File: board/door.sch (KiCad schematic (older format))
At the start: 16 parts

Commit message: Finish first draft of schematic
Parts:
- removed C? (x2): C, symbol C
- removed D?: D_Photo, symbol D_Photo
- added C100u1, C? (x2): C, symbol C
- added D1: LED, symbol LED
- added J1: Conn_01x06, symbol Conn_01x06
- added R1: 10, symbol R
- added R2, R3, R5: R, symbol R
- added R4: R_PHOTO, symbol R_PHOTO
- added RV1: POT, symbol POT
- added U2: BA6287F-E2, symbol BA6287F-E2
- gave numbers to parts that had none: 13
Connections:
- net labels added: +5V, BOTTOM, FORWARD, GND, LED, LIGHT_SENS, MINUS, MISO, MODE, MOSI, OK, PLUS, REVERSE, SCK, TOP, XTAL1, XTAL2, ~RESET
- wire segments 0 -> 92
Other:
- note added: "32.786 kHz Crystal"
- note added: "4-Button Panel"
- note added: "General LED"
- note added: "ISP"
- note added: "LCD"
- note added: "Light Sensor"
- note added: "Magnetic Switches"
- note added: "Motor driver and DC Motor"
- note added: "Power Supply"
- moved on the sheet: BT1, C1, M1, SW_BOTTOM1, SW_MINUS1, SW_MODE1, SW_OK1, SW_PLUS1, SW_TOP1, U1, U3, U4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

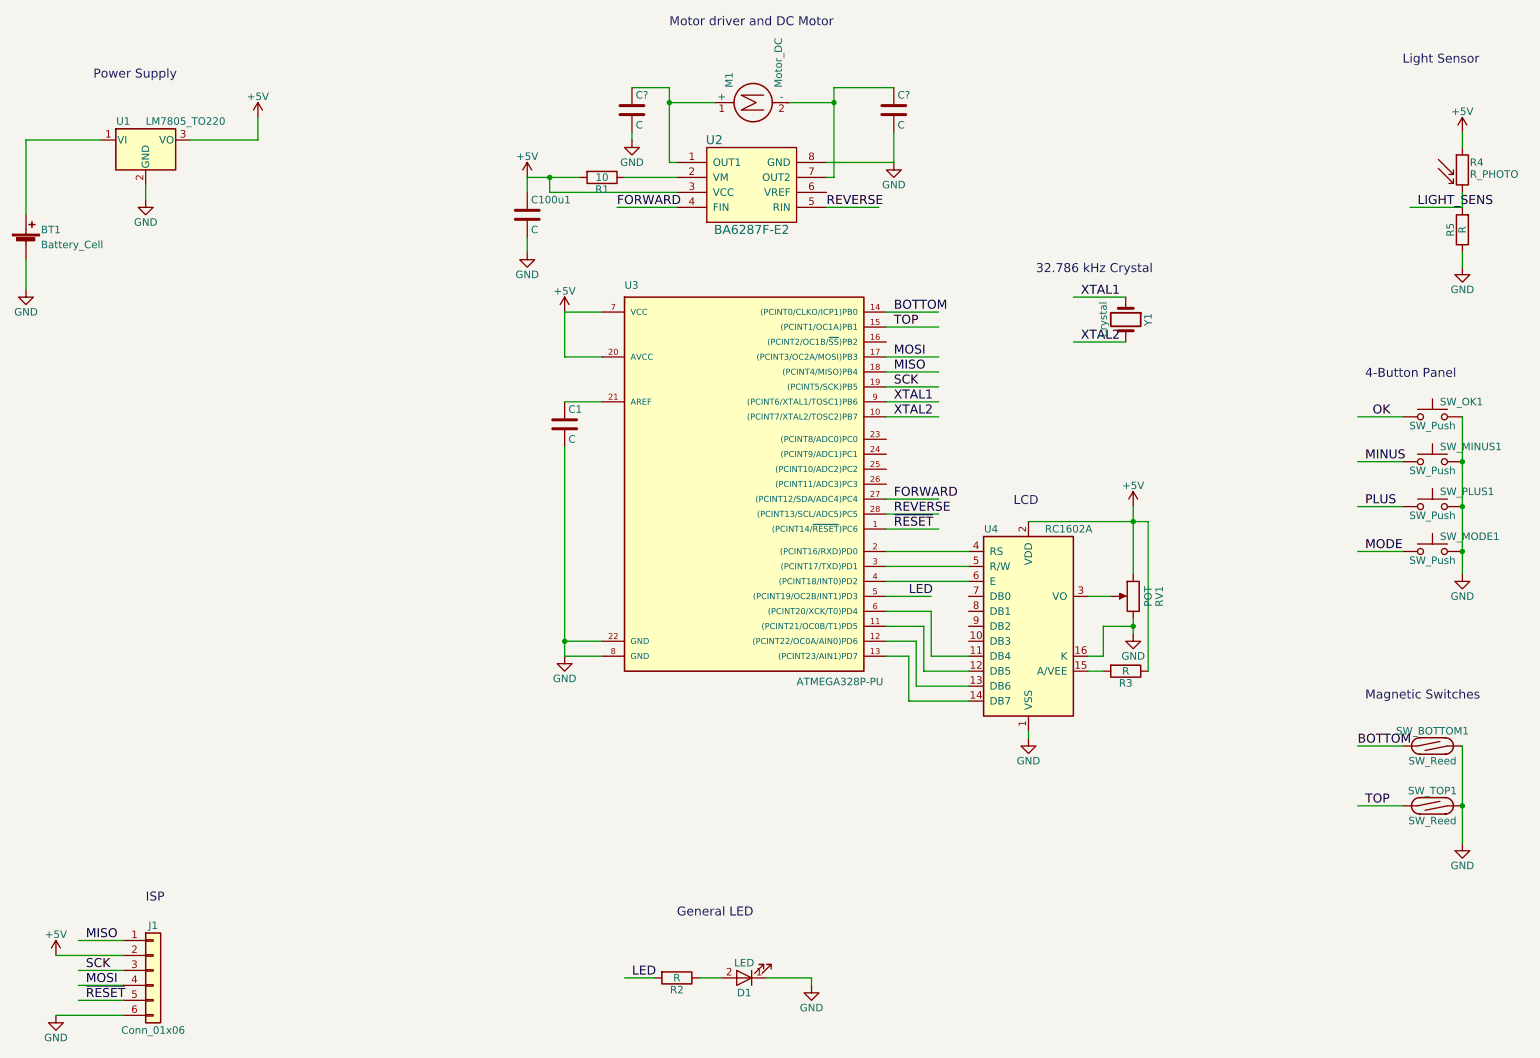
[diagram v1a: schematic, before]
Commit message: add schematic (missing)
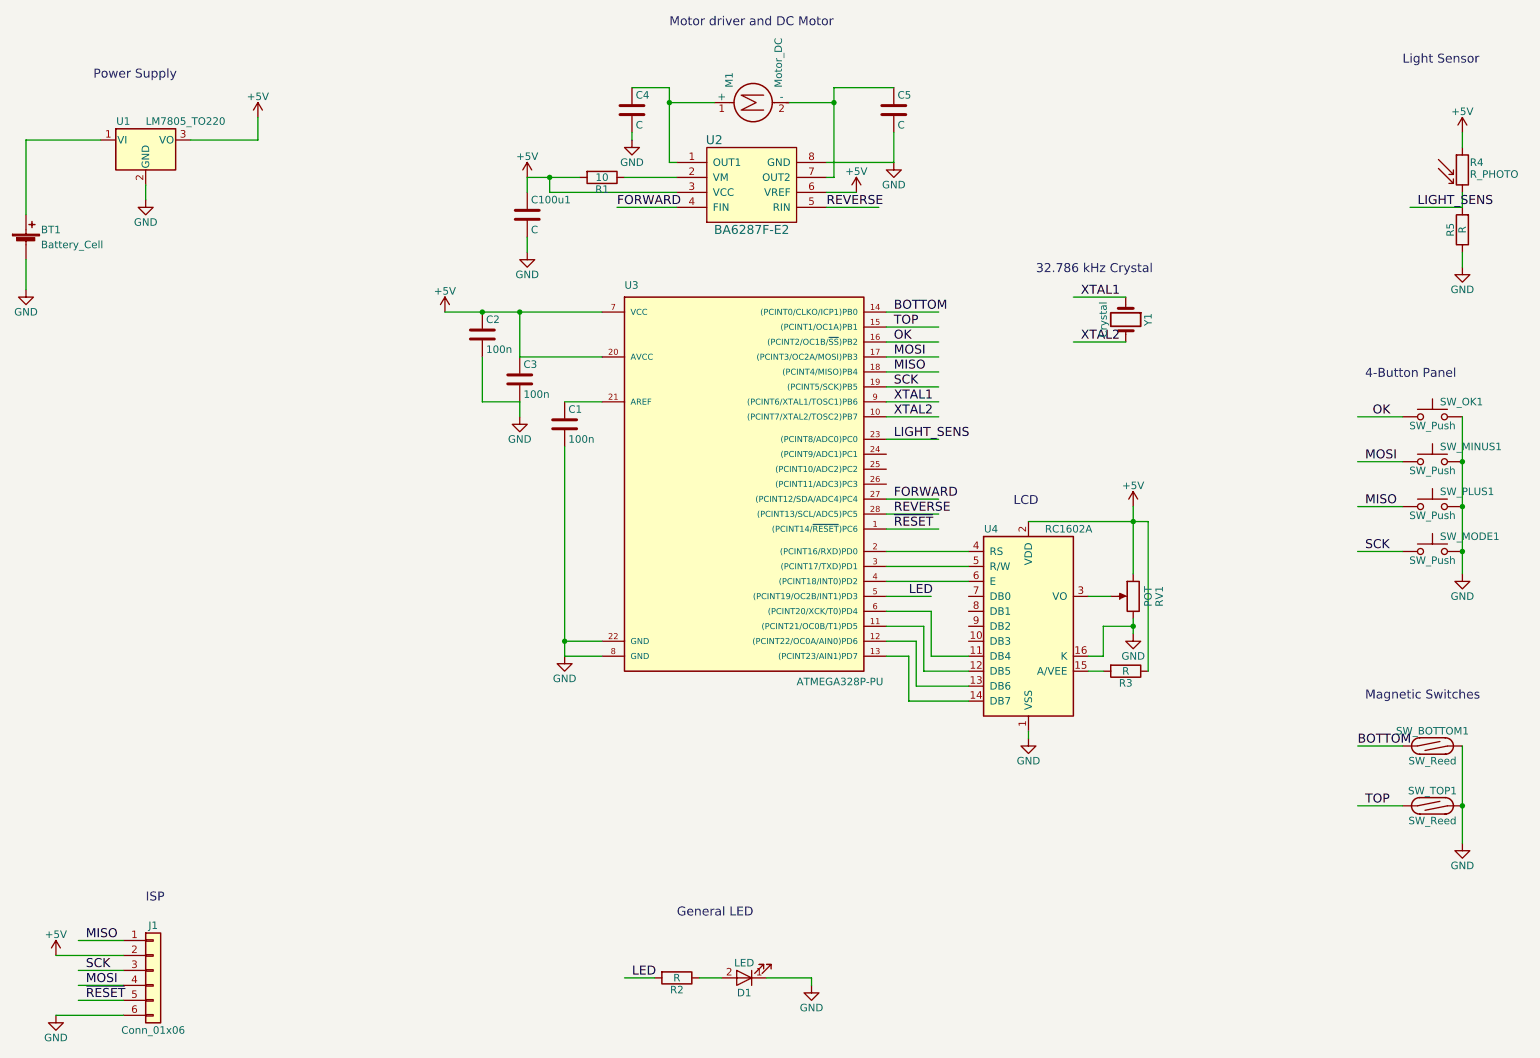
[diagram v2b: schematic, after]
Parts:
- added C2, C3: 100n, symbol C
- C1: value C -> 100n
- gave numbers to parts that had none: 2
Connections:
- net labels removed: MINUS, MODE, PLUS
- wire segments 92 -> 98
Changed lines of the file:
@@
 P 4500 3250
 F 0 "C1" H 4525 3350 50  0000 L CNN
-F 1 "C" H 4525 3150 50  0000 L CNN
+F 1 "100n" H 4525 3150 50  0000 L CNN
 F 2 "" H 4538 3100 50  0001 C CNN
 F 3 "" H 4500 3250 50  0001 C CNN
@@
 Wire Wire Line
 	6650 4300 7200 4300
-Wire Wire Line
-	8150 4400 8000 4400
 $Comp
 L GND #PWR03
@@
 	8300 4550 8300 4650
 Wire Wire Line
-	8100 4900 8000 4900
-Wire Wire Line
 	8000 4800 8100 4800
 Wire Wire Line
@@
 Wire Wire Line
 	4900 6950 5100 6950
-Wire Wire Line
-	7600 5300 7600 5350
 Text Label 4950 6950 0    60   ~ 0
 LED
-Wire Wire Line
-	900  1850 900  1350
-Wire Wire Line
-	900  1350 1400 1350
 $Comp
 L GND #PWR07
@@
 L +5V #PWR010
 U 1 1 5B279F52
-P 4500 2500
-F 0 "#PWR010" H 4500 2350 50  0001 C CNN
-F 1 "+5V" H 4500 2640 50  0000 C CNN
-F 2 "" H 4500 2500 50  0001 C CNN
-F 3 "" H 4500 2500 50  0001 C CNN
-	1    4500 2500
-	1    0    0    -1
-$EndComp
-Wire Wire Line
-	4750 2500 4500 2500
-Wire Wire Line
-	4750 2800 4500 2800
-Wire Wire Line
-	4500 2800 4500 2500
+P 3700 2500
+F 0 "#PWR010" H 3700 2350 50  0001 C CNN
+F 1 "+5V" H 3700 2640 50  0000 C CNN
+F 2 "" H 3700 2500 50  0001 C CNN
+F 3 "" H 3700 2500 50  0001 C CNN
+	1    3700 2500
+	1    0    0    -1
+$EndComp
+Wire Wire Line
+	4200 2800 4750 2800
 Wire Wire Line
 	6250 1500 6700 1500
@@
 OK
 Text Label 9850 3500 0    60   ~ 0
-MINUS
+MOSI
 Text Label 9850 3800 0    60   ~ 0
-PLUS
+MISO
 Text Label 9850 4100 0    60   ~ 0
-MODE
+SCK
 Wire Wire Line
 	1550 6700 1250 6700
@@
 	0    1    1    0
 $EndComp
-Wire Wire Line
-	4900 1600 5250 1600
 Wire Wire Line
 	4250 1600 4600 1600
@@
 Magnetic Switches
 $Comp
-L C C?
+L C C4
 U 1 1 5B28EE99
 P 4950 1150
-F 0 "C?" H 4975 1250 50  0000 L CNN
+F 0 "C4" H 4975 1250 50  0000 L CNN
 F 1 "C" H 4975 1050 50  0000 L CNN
 F 2 "" H 4988 1000 50  0001 C CNN
@@
 $EndComp
 $Comp
-L C C?
+L C C5
 U 1 1 5B28EF76
 P 6700 1150
-F 0 "C?" H 6725 1250 50  0000 L CNN
+F 0 "C5" H 6725 1250 50  0000 L CNN
 F 1 "C" H 6725 1050 50  0000 L CNN
 F 2 "" H 6738 1000 50  0001 C CNN
@@
 $EndComp
 $Comp
-L GND #PWR?
+L GND #PWR018
 U 1 1 5B28F12C
 P 4950 1350
-F 0 "#PWR?" H 4950 1100 50  0001 C CNN
+F 0 "#PWR018" H 4950 1100 50  0001 C CNN
 F 1 "GND" H 4950 1200 50  0000 C CNN
 F 2 "" H 4950 1350 50  0001 C CNN
@@
 $EndComp
 Wire Wire Line
-	4950 1300 4950 1350
-Wire Wire Line
 	4950 1000 5200 1000
 Connection ~ 5200 1100
@@
 	4500 3100 4750 3100
 $Comp
-L GND #PWR?
+L GND #PWR019
 U 1 1 5B28F5CD
 P 4500 4800
-F 0 "#PWR?" H 4500 4550 50  0001 C CNN
+F 0 "#PWR019" H 4500 4550 50  0001 C CNN
 F 1 "GND" H 4500 4650 50  0000 C CNN
 F 2 "" H 4500 4800 50  0001 C CNN
@@
 	4500 3400 4500 4800
 Connection ~ 4500 4700
+Wire Wire Line
+	7000 3350 6650 3350
+$Comp
+L +5V #PWR020
+U 1 1 5B2A0858
+P 6450 1700
+F 0 "#PWR020" H 6450 1550 50  0001 C CNN
+F 1 "+5V" H 6450 1840 50  0000 C CNN
+F 2 "" H 6450 1700 50  0001 C CNN
+F 3 "" H 6450 1700 50  0001 C CNN
+	1    6450 1700
+	1    0    0    -1
+$EndComp
+Wire Wire Line
+	6250 1700 6450 1700
+Wire Wire Line
+	6650 2700 7000 2700
+Text Label 6700 2700 0    60   ~ 0
+OK
+Text Label 6700 3350 0    60   ~ 0
+LIGHT_SENS
+$Comp
+L C C2
+U 1 1 5B2A24F8
+P 3950 2650
+F 0 "C2" H 3975 2750 50  0000 L CNN
+F 1 "100n" H 3975 2550 50  0000 L CNN
+F 2 "" H 3988 2500 50  0001 C CNN
+F 3 "" H 3950 2650 50  0001 C CNN
+	1    3950 2650
+	1    0    0    -1
+$EndComp
+$Comp
+L C C3
+U 1 1 5B2A25A0
+P 4200 2950
+F 0 "C3" H 4225 3050 50  0000 L CNN
+F 1 "100n" H 4225 2850 50  0000 L CNN
+F 2 "" H 4238 2800 50  0001 C CNN
+F 3 "" H 4200 2950 50  0001 C CNN
+	1    4200 2950
+	1    0    0    -1
+$EndComp
+Wire Wire Line
+	3700 2500 4750 2500
+Connection ~ 3950 2500
+Wire Wire Line
+	4200 2800 4200 2500
+Connection ~ 4200 2500
+$Comp
+L GND #PWR021
+U 1 1 5B2A290C
+P 4200 3200
+F 0 "#PWR021" H 4200 2950 50  0001 C CNN
+F 1 "GND" H 4200 3050 50  0000 C CNN
+F 2 "" H 4200 3200 50  0001 C CNN
+F 3 "" H 4200 3200 50  0001 C CNN
+	1    4200 3200
+	1    0    0    -1
+$EndComp
+Wire Wire Line
+	3950 2800 3950 3100
+Wire Wire Line
+	3950 3100 4200 3100
+Wire Wire Line
+	4200 3100 4200 3200
+Wire Wire Line
+	7600 5300 7600 5350
+Wire Wire Line
+	8000 4400 8150 4400
+Wire Wire Line
+	8000 4900 8100 4900
+Wire Wire Line
+	4900 1600 5250 1600
+Wire Wire Line
+	4950 1350 4950 1300
+Wire Wire Line
+	900  1850 900  1350
+Wire Wire Line
+	900  1350 1400 1350
 $EndSCHEMATC
